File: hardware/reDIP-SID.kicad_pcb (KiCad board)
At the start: 6 copper layers, 17.8 x 35.6 mm, 92 parts, among them J1 Conn_01x04, J2 Conn_01x04, J3 Conn_01x10, J4 Conn_01x10, J5 TYPE-C-31-M-12, J6 Conn_02x05_Odd_Even, Q1 PDTA143ZMB, SW1 KXT331LHS, U1 NCP163AMX120TBG, U2 NCP167AMX330TBG, U3 SN74CBTD16211DGVR, U4 SGTL5000XNLA3, U5 NUF2042XV6, U6 APS6404L-3SQR-SN, U7 W25Q128JVPIM, U8 ICE40UP5K-SG48I, X1 ASCO-24.576MHZ-EK-T

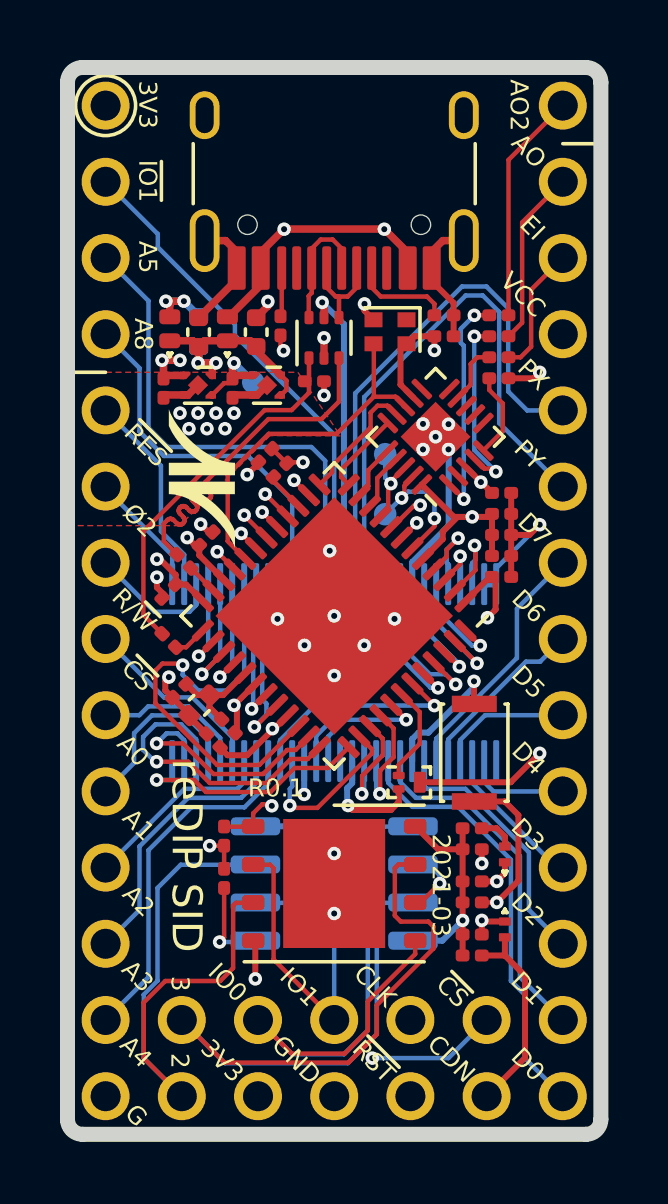
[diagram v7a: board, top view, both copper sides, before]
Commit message: Attempt at reducing layer count from 6 to 4
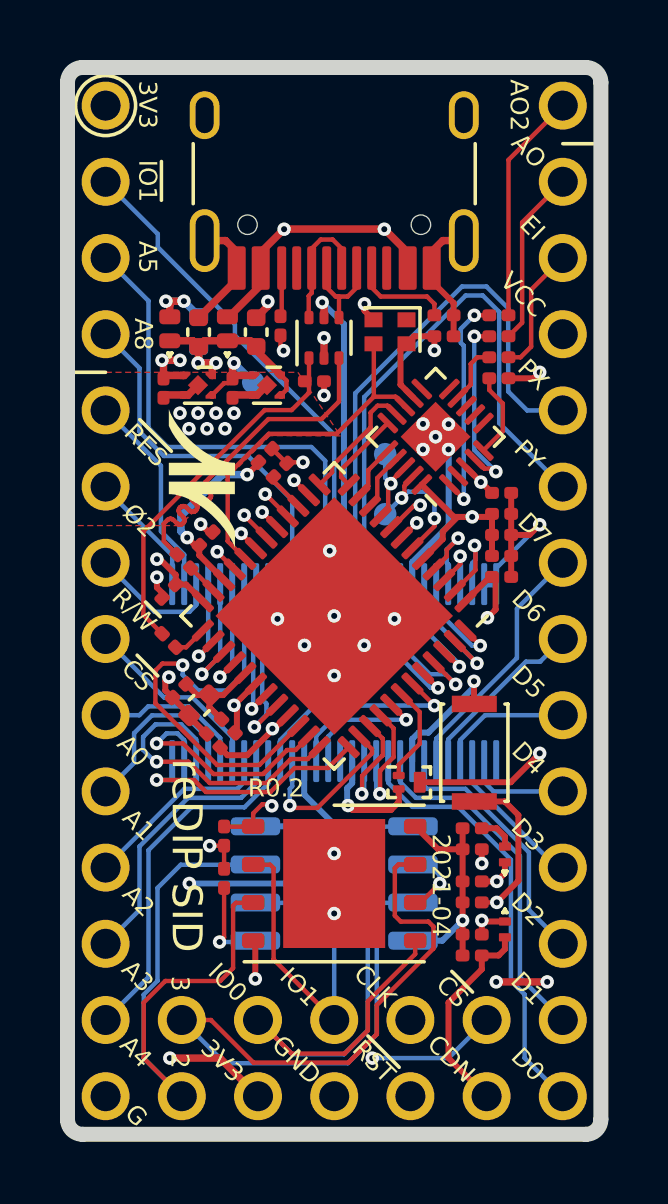
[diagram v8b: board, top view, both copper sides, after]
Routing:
- net +3V3: track 27.2 -> 37.3 mm, vias 11 -> 14
- net +5V: track 29.1 -> 38.6 mm
- net +1V2: track 30.9 -> 35.0 mm
- added copper zone on In2.Cu, net +1V2
- added copper zone on In2.Cu, net +3V3
- added copper zone on B.Cu, net GND
- added copper zone on In2.Cu, net VBUS
- added copper zone on In2.Cu, net VCC
- removed copper zone on In3.Cu, net +1V2
- removed copper zone on In3.Cu, net +3V3
- removed copper zone on In4.Cu, net GND
- removed copper zone on In3.Cu, net VBUS
- removed copper zone on In3.Cu, net VCC
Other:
- copper layers 6 -> 4
- board text added: "2021-04"
- board text added: "R0.2"
- board text removed: "2021-03"
- board text removed: "R0.1"
